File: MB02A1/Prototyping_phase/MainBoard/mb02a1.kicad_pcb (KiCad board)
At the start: 2 copper layers, 71 parts, among them J1 USB_B_Mini, J2 USB_B_Mini, J3 USB_B_Mini, J4 USB_B_Mini, Q1 BC369, Q2 BC369, U1 CH340G, U2 CH340G, U3 CH340G, U4 AMS1117-3.3, U5 W25Q64JVS, U6 25LC256, U7 25LC640, U8 NUCLEO-F446RE, X1 12MHz, X2 12MHz, X3 12MHz

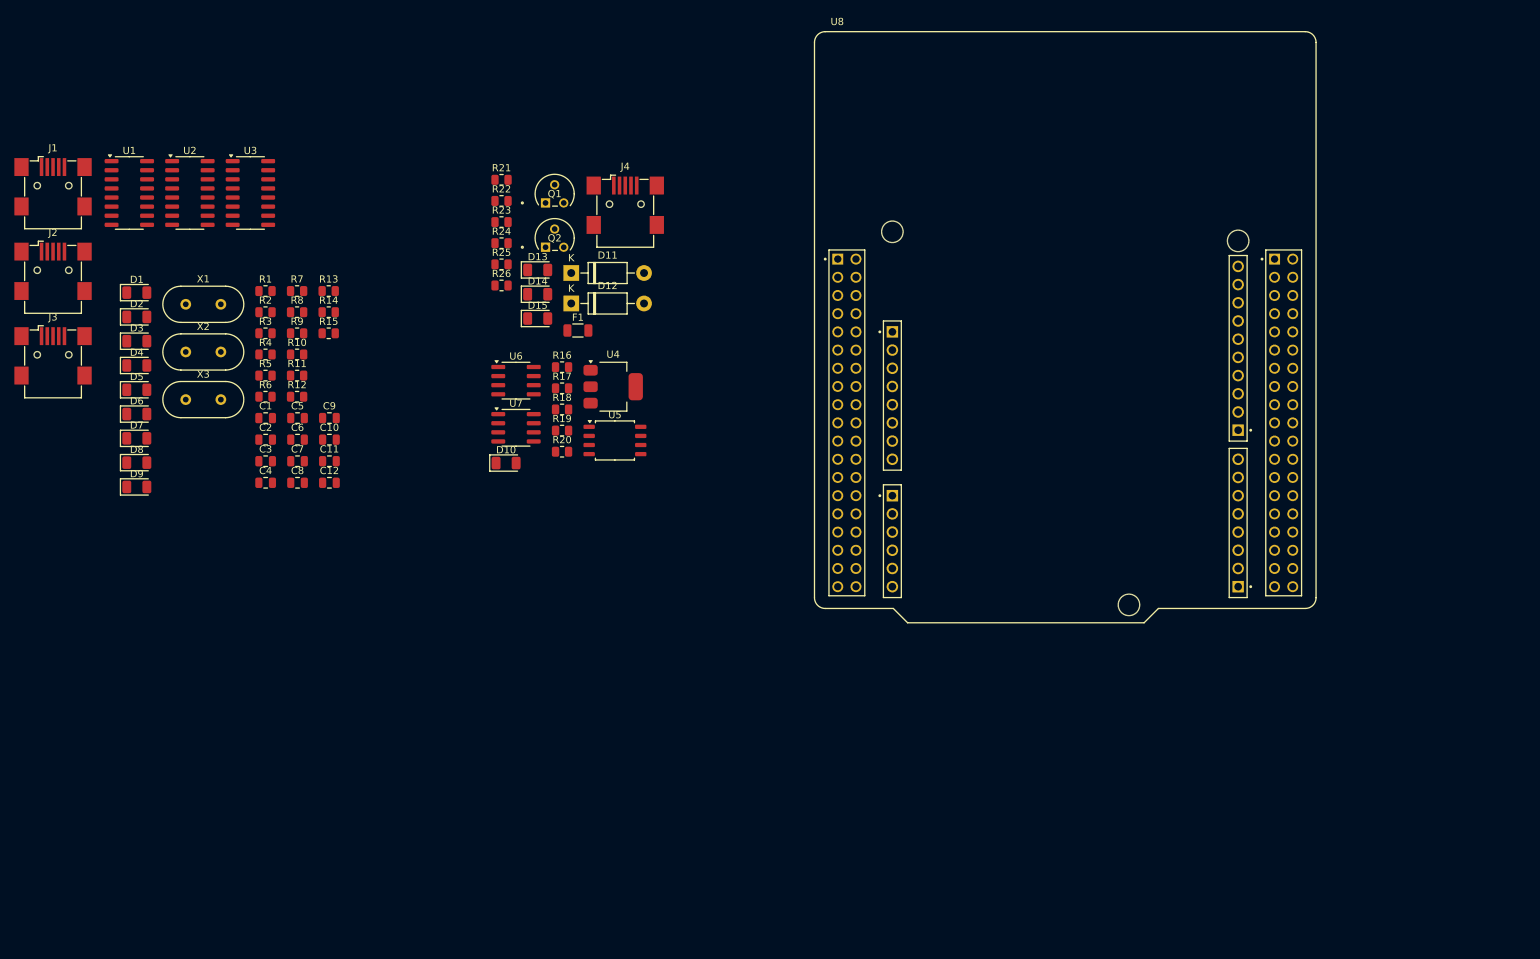
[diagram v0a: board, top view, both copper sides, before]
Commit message: Datasheets added, design updated.
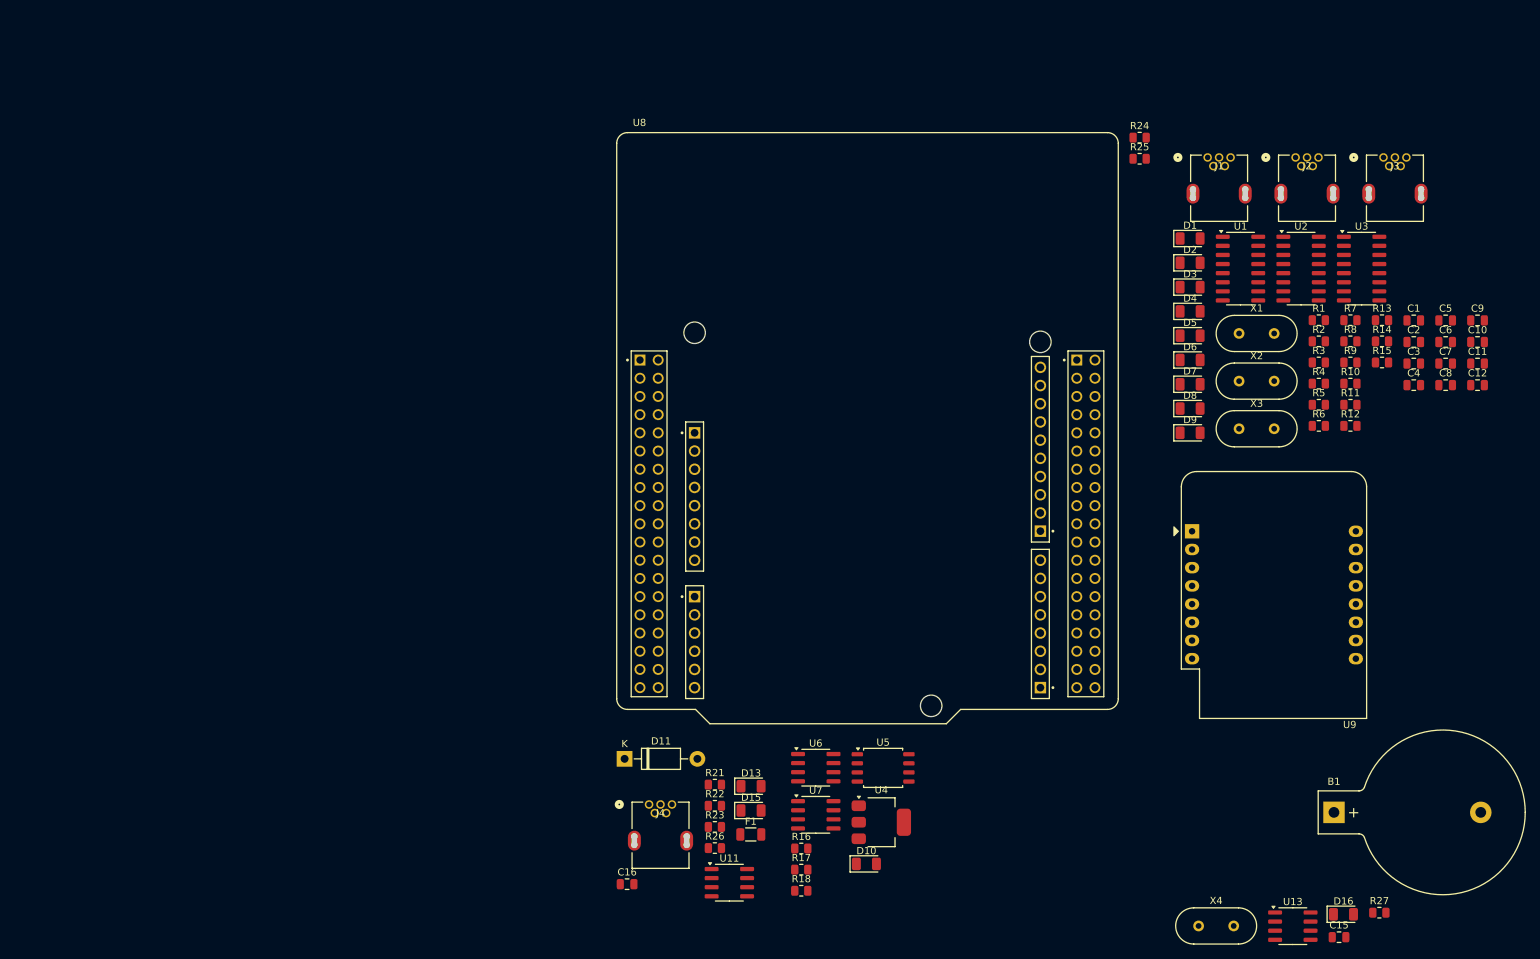
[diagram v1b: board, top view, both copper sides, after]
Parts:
- removed D12: ZY5.6, Diode_THT:D_DO-41_SOD81_P10.16mm_Horizontal
- removed D14: LED, LED_SMD:LED_1206_3216Metric
- removed Q1, Q2: BC369, footprints:TO-92_ONS
- removed R19: 1k, Resistor_SMD:R_0805_2012Metric
- removed R20: 2k, Resistor_SMD:R_0805_2012Metric
- added B1: BC2032-E2, Battery:BatteryHolder_Keystone_103_1x20mm, F.Cu at (251.8, 135.0)
- added C15: 100p, Capacitor_SMD:C_0805_2012Metric, F.Cu at (252.5, 152.4)
- added C16: 1n, Capacitor_SMD:C_0805_2012Metric, F.Cu at (153.1, 145.0)
- added D16: D_Schottky, Diode_SMD:D_1206_3216Metric, F.Cu at (253.1, 149.2)
- added R27: 1k, Resistor_SMD:R_0805_2012Metric, F.Cu at (258.1, 149.0)
- added U11: ACS712-05B, Package_SO:SOIC-8_3.9x4.9mm_P1.27mm, F.Cu at (167.4, 144.8)
- added U13: DS1307Z+, Package_SO:SOIC-8_3.9x4.9mm_P1.27mm, F.Cu at (246.0, 150.9)
- added U9: WEMOS_D1_mini, RF_Module:WEMOS_D1_mini_light, F.Cu at (231.9, 95.8)
- added X4: 32.768 kHz, Crystal:Crystal_HC18-U_Vertical, F.Cu at (232.9, 150.8)
- J1, J2, J3, J4: value USB_B_Mini -> USB B mini; footprint Connector_USB:USB_Mini-B_Wuerth_65100516121_Horizontal -> USB_B_mini_th:54819-0519_MOL
- R22: value 220R -> 10k
- R23: value 2k7 -> 10k
- R24: value 6k8 -> 4k7
- R25: value 470R -> 4k7
- moved J3 187.7 mm to (258.7, 43.6)
- moved J2 174.1 mm to (246.4, 43.6)
- moved J1 161.2 mm to (234.1, 43.6)
- moved C10 160.8 mm to (271.8, 69.3)
- moved C11 160.8 mm to (271.8, 72.4)
- moved C12 160.8 mm to (271.8, 75.4)
- moved C9 160.8 mm to (271.8, 66.3)
- moved C1 160.8 mm to (262.9, 66.3)
- moved C2 160.8 mm to (262.9, 69.3)
- moved C3 160.8 mm to (262.9, 72.4)
- moved C4 160.8 mm to (262.9, 75.4)
- moved C5 160.8 mm to (267.3, 66.3)
- moved C6 160.8 mm to (267.3, 69.3)
- moved C7 160.8 mm to (267.3, 72.4)
- moved C8 160.8 mm to (267.3, 75.4)
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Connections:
- net W25Q64_NCS0V3 renamed W25Q64_NCS3V3
- D10 pad 2: P5V_MEM -> M5V
- J1 pad 6: unconnected-(J1-Shield-Pad6) -> (no net)
- J2 pad 6: unconnected-(J2-Shield-Pad6) -> (no net)
- J3 pad 6: unconnected-(J3-Shield-Pad6) -> (no net)
- J4 pad 6: unconnected-(J4-Shield-Pad6) -> (no net)
- R22 pad 1: Net-(D12-K) -> U_PWR_MEAS
- R22 pad 2: Net-(D14-A) -> Net-(D11-K)
- R23 pad 1: Net-(D12-K) -> GND
- R23 pad 2: Net-(D11-K) -> U_PWR_MEAS
- R24 pad 1: Net-(D12-K) -> M5V
- R24 pad 2: Net-(Q1-B) -> I2C1_SDA
- R25 pad 1: GND -> M5V
- R25 pad 2: Net-(Q1-C) -> I2C1_SCL
- U4 pad 3: P5V_MEM -> M5V
- U5 pad 7: W25Q64_NRST0V3 -> Net-(U4-VO)
- U6 pad 3: P5V_MEM -> M5V
- U6 pad 7: 25LC256_NRST -> M5V
- U6 pad 8: P5V_MEM -> M5V
- U7 pad 3: P5V_MEM -> M5V
- U7 pad 7: 25LC640_NRST -> M5V
- U7 pad 8: P5V_MEM -> M5V
- U8 pad CN10_17: unconnected-(U8B-PB6-PadCN10_17) -> I2C1_SCL
- U8 pad CN10_19: unconnected-(U8B-PC7-PadCN10_19) -> SPI2_SCK
- U8 pad CN10_21: unconnected-(U8B-PA9-PadCN10_21) -> USART1_TX
- U8 pad CN10_22: unconnected-(U8B-PB2-PadCN10_22) -> 25LC256_NCS
- U8 pad CN10_24: unconnected-(U8B-PB1-PadCN10_24) -> 25LC640_NCS
- U8 pad CN10_28: unconnected-(U8B-PB14-PadCN10_28) -> WEMOS_RST
- U8 pad CN10_33: unconnected-(U8B-PA10-PadCN10_33) -> USART1_RX
- U8 pad CN6_5: unconnected-(U8C-CN6_+5V-PadCN6_5) -> M5V
- U8 pad CN7_19: Net-(U8A-CN7_GND-PadCN7_19) -> GND
- U8 pad CN7_20: Net-(U8A-CN7_GND-PadCN7_19) -> GND
- U8 pad CN7_21: unconnected-(U8A-PB7-PadCN7_21) -> I2C1_SDA
- U8 pad CN7_22: Net-(U8A-CN7_GND-PadCN7_19) -> GND
- U8 pad CN7_28: unconnected-(U8A-PA0-PadCN7_28) -> UART4_TX
- U8 pad CN7_3: unconnected-(U8A-PC12-PadCN7_3) -> UART5_TX
- U8 pad CN7_30: unconnected-(U8A-PA1-PadCN7_30) -> UART4_RX
- U8 pad CN7_34: unconnected-(U8A-PB0-PadCN7_34) -> W25Q64_NCS
- U8 pad CN7_35: unconnected-(U8A-PC2-PadCN7_35) -> SPI2_MISO
- U8 pad CN7_36: unconnected-(U8A-PC1/PB9-PadCN7_36) -> SPI2_MOSI
- U8 pad CN7_37: unconnected-(U8A-PC3-PadCN7_37) -> I_PWR_MEAS
- U8 pad CN7_38: unconnected-(U8A-PC0/PB8-PadCN7_38) -> U_PWR_MEAS
- U8 pad CN7_4: unconnected-(U8A-PD2-PadCN7_4) -> UART5_RX
- U8 pad CN7_6: unconnected-(U8A-E5V-PadCN7_6) -> 5V_REG
- U8 pad CN7_8: Net-(U8A-CN7_GND-PadCN7_19) -> GND
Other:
- board outline added: 7.3 x 1.2 mm

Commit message: Design update, production preparation.
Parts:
- removed C15: 100p, Capacitor_SMD:C_0805_2012Metric
- removed C16: 1n, Capacitor_SMD:C_0805_2012Metric
- removed D16: D_Schottky, Diode_SMD:D_1206_3216Metric
- removed R27: 1k, Resistor_SMD:R_0805_2012Metric
- removed U13: DS1307Z+, Package_SO:SOIC-8_3.9x4.9mm_P1.27mm
- removed X4: 32.768 kHz, Crystal:Crystal_HC18-U_Vertical
- added ?: , , F.Cu at (80.5, 49.7)
- added ?: , , F.Cu at (80.5, 150.0)
- added ?: , , F.Cu at (205.8, 150.0)
- added ?: , , F.Cu at (205.8, 50.0)
- added ADC.1: Conn_01x02_Pin, Connector_PinHeader_2.54mm:PinHeader_1x02_P2.54mm_Vertical, F.Cu at (199.0, 83.8)
- added ADC.2: Conn_01x02_Pin, Connector_PinHeader_2.54mm:PinHeader_1x02_P2.54mm_Vertical, F.Cu at (204.8, 83.8)
- added C13: 100n, Capacitor_SMD:C_0805_2012Metric, F.Cu at (126.2, 94.6)
- added D12: LED, LED_SMD:LED_1206_3216Metric, F.Cu at (81.6, 143.9)
- added D14: LED, LED_SMD:LED_1206_3216Metric, F.Cu at (100.1, 147.5)
- added DAC.1: Conn_01x02_Pin, Connector_PinHeader_2.54mm:PinHeader_1x02_P2.54mm_Vertical, F.Cu at (198.8, 63.5)
- added DISPLAY1: Conn_01x14_Pin, Connector_PinHeader_2.54mm:PinHeader_1x14_P2.54mm_Vertical, F.Cu at (193.0, 53.3)
- added EXIO.1: Conn_01x08_Pin, Connector_PinHeader_2.54mm:PinHeader_1x08_P2.54mm_Vertical, F.Cu at (204.3, 128.7)
- added EXIO.2: Conn_01x08_Pin, Connector_PinHeader_2.54mm:PinHeader_1x08_P2.54mm_Vertical, F.Cu at (204.3, 134.9)
- added EXTI.1: Conn_01x02_Pin, Connector_PinHeader_2.54mm:PinHeader_1x02_P2.54mm_Vertical, F.Cu at (204.8, 63.5)
- added EXTI.2: Conn_01x02_Pin, Connector_PinHeader_2.54mm:PinHeader_1x02_P2.54mm_Vertical, F.Cu at (198.8, 73.8)
- added EXTI.3: Conn_01x02_Pin, Connector_PinHeader_2.54mm:PinHeader_1x02_P2.54mm_Vertical, F.Cu at (204.8, 73.8)
- added I2C1.1: Conn_01x04_Pin, Connector_PinHeader_2.54mm:PinHeader_1x04_P2.54mm_Vertical, F.Cu at (178.8, 128.9)
- added I2C1.2: Conn_01x04_Pin, Connector_PinHeader_2.54mm:PinHeader_1x04_P2.54mm_Vertical, F.Cu at (178.8, 134.9)
- added I2C1.3: Conn_01x04_Pin, Connector_PinHeader_2.54mm:PinHeader_1x04_P2.54mm_Vertical, F.Cu at (178.8, 140.9)
- added I2C1.4: Conn_01x04_Pin, Connector_PinHeader_2.54mm:PinHeader_1x04_P2.54mm_Vertical, F.Cu at (178.8, 146.9)
- added PWM.1: Conn_01x02_Pin, Connector_PinHeader_2.54mm:PinHeader_1x02_P2.54mm_Vertical, F.Cu at (193.2, 116.0)
- added PWM.2: Conn_01x02_Pin, Connector_PinHeader_2.54mm:PinHeader_1x02_P2.54mm_Vertical, F.Cu at (199.0, 116.0)
- added PWM.3: Conn_01x02_Pin, Connector_PinHeader_2.54mm:PinHeader_1x02_P2.54mm_Vertical, F.Cu at (204.8, 116.0)
- added PWR3V3.1: Conn_01x02_Pin, Connector_PinHeader_2.54mm:PinHeader_1x02_P2.54mm_Vertical, F.Cu at (193.2, 105.2)
- added PWR3V3.2: Conn_01x02_Pin, Connector_PinHeader_2.54mm:PinHeader_1x02_P2.54mm_Vertical, F.Cu at (199.0, 105.3)
- added PWR3V3.3: Conn_01x02_Pin, Connector_PinHeader_2.54mm:PinHeader_1x02_P2.54mm_Vertical, F.Cu at (204.8, 105.3)
- added PWR5V.1: Conn_01x02_Pin, Connector_PinHeader_2.54mm:PinHeader_1x02_P2.54mm_Vertical, F.Cu at (193.2, 94.5)
- added PWR5V.2: Conn_01x02_Pin, Connector_PinHeader_2.54mm:PinHeader_1x02_P2.54mm_Vertical, F.Cu at (199.0, 94.5)
- added PWR5V.3: Conn_01x02_Pin, Connector_PinHeader_2.54mm:PinHeader_1x02_P2.54mm_Vertical, F.Cu at (204.8, 94.5)
- added R19: 1k5, Resistor_SMD:R_0805_2012Metric, F.Cu at (87.6, 135.6)
- added R20: 1k, Resistor_SMD:R_0805_2012Metric, F.Cu at (161.8, 97.8)
- added SPI2.1: Conn_01x06_Pin, Connector_PinHeader_2.54mm:PinHeader_1x06_P2.54mm_Vertical, F.Cu at (199.1, 140.9)
- added SPI2.2: Conn_01x06_Pin, Connector_PinHeader_2.54mm:PinHeader_1x06_P2.54mm_Vertical, F.Cu at (199.1, 147.0)
- added U10: WEMOS_D1_mini, RF_Module:WEMOS_D1_mini_light, F.Cu at (114.8, 147.5)
- added U12: MCP23017_SO, Package_SO:SOIC-28W_7.5x17.9mm_P1.27mm, F.Cu at (167.8, 73.4)
- C1: value 22p -> 1n
- C10, C9: value 22p -> 100n
- C3, C4, C7: value 100n -> 22p
- D11: value 1N4001 -> LED; footprint Diode_THT:D_DO-41_SOD81_P10.16mm_Horizontal -> LED_SMD:LED_1206_3216Metric
- D2: value LED -> 1N4001; footprint LED_SMD:LED_1206_3216Metric -> Diode_THT:D_DO-41_SOD81_P10.16mm_Horizontal
- R1: value 1k5 -> 220R
- R17: value 1k -> 1k5
- R18: value 2k -> 1k5
- R2, R3: value 1k5 -> 10k
- R21: value 220R -> 2k
- R22, R23: value 10k -> 4k7
- R24, R25: value 4k7 -> 1k5
- U1: value CH340G -> ACS712-05B; footprint Package_SO:SOIC-16_3.9x9.9mm_P1.27mm -> Package_SO:SOIC-8_3.9x4.9mm_P1.27mm
- U11: value ACS712-05B -> DS3231M; footprint Package_SO:SOIC-8_3.9x4.9mm_P1.27mm -> Package_SO:SOIC-16W_7.5x10.3mm_P1.27mm
- U4: value AMS1117-3.3 -> CH340G; footprint Package_TO_SOT_SMD:SOT-223-3_TabPin2 -> Package_SO:SOIC-16_3.9x9.9mm_P1.27mm
- U5: value W25Q64JVS -> AMS1117-3.3; footprint Package_SO:SOIC-8_5.23x5.23mm_P1.27mm -> Package_TO_SOT_SMD:SOT-223-3_TabPin2
- U6: value 25LC256 -> W25Q64JVS; footprint Package_SO:SOIC-8_3.9x4.9mm_P1.27mm -> Package_SO:SOIC-8_5.23x5.23mm_P1.27mm
- U7: value 25LC640 -> 25LC256
- U8: value NUCLEO-F446RE -> 25LC640; footprint NUCLEO-F446RE:MODULE_NUCLEO-F446RE -> Package_SO:SOIC-8_3.9x4.9mm_P1.27mm
- U9: value WEMOS_D1_mini -> NUCLEO-F446RE; footprint RF_Module:WEMOS_D1_mini_light -> NUCLEO-F446RE:MODULE_NUCLEO-F446RE
- X1, X2, X3: value 12MHz -> 12 MHz; footprint Crystal:Crystal_HC18-U_Vertical -> Crystal:Crystal_HC49-U_Vertical
- moved C7 188.1 mm to (93.4, 143.9)
- moved R13 186.0 mm to (87.6, 139.9)
- moved C6 180.8 mm to (93.4, 118.7)
- moved J3 180.7 mm to (87.3, 101.0), turned to -90 degrees
- moved R15 177.1 mm to (87.6, 118.9)
- moved C5 176.1 mm to (93.4, 93.7)
- moved R14 172.5 mm to (87.7, 93.9)
- moved C1 170.3 mm to (92.7, 68.9)
- moved R12 169.8 mm to (87.6, 114.9)
- moved R11 166.6 mm to (87.8, 90.1)
- moved U3 163.9 mm to (97.7, 102.9)
- moved D6 163.1 mm to (81.6, 135.6)
- moved R4 162.4 mm to (87.6, 64.9)
- moved J2 162.4 mm to (87.3, 75.9), turned to -90 degrees
- moved R1 162.1 mm to (87.6, 68.9)
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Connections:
- B1 pad 1: Net-(D16-A) -> Net-(U11-VBAT)
- C1 pad 1: Net-(U1-XI) -> Net-(U1-FILTER)
- C10 pad 1: Net-(U3-XO) -> Net-(U4-V3)
- C11 pad 1: Net-(U3-V3) -> VBUS1
- C12 pad 1: VBUS3 -> VBUS2
- C2 pad 1: Net-(U1-XO) -> Net-(U2-XI)
- C3 pad 1: Net-(U1-V3) -> Net-(U3-XI)
- C4 pad 1: VBUS1 -> Net-(U4-XI)
- C5 pad 1: Net-(U2-XI) -> Net-(U2-XO)
- C6 pad 1: Net-(U2-XO) -> Net-(U3-XO)
- C7 pad 1: Net-(U2-V3) -> Net-(U4-XO)
- C8 pad 1: VBUS2 -> Net-(U2-V3)
- C9 pad 1: Net-(U3-XI) -> Net-(U3-V3)
- D1 pad 2: VBUS1 -> Net-(D1-A)
- D10 pad 2: M5V -> VBUS1
- D11 pad 2: GND -> VBUS2
- D13 pad 1: Net-(D11-K) -> Net-(D13-K)
- D15 pad 2: 5V_REG -> Net-(D15-A)
- D2 pad 1: Net-(D2-K) -> Net-(D1-K)
- D2 pad 2: VBUS1 -> GND
- D3 pad 2: VBUS1 -> 5V_REG
- D4 pad 2: VBUS2 -> VBUS1
- D6 pad 2: VBUS2 -> VBUS3
- D7 pad 2: VBUS3 -> VBUS1
- D8 pad 2: VBUS3 -> VBUS2
- F1 pad 1: Net-(J4-VBUS) -> Net-(J1-VBUS)
- F1 pad 2: Net-(D11-K) -> Net-(D1-K)
- J1 pad 1: VBUS1 -> Net-(J1-VBUS)
- J1 pad 2: D1- -> unconnected-(J1-D--Pad2)
- J1 pad 3: D1+ -> unconnected-(J1-D+-Pad3)
- J2 pad 1: VBUS2 -> VBUS1
- J2 pad 2: D2- -> D1-
- J2 pad 3: D2+ -> D1+
- J3 pad 1: VBUS3 -> VBUS2
- J3 pad 2: D3- -> D2-
- J3 pad 3: D3+ -> D2+
- J4 pad 1: Net-(J4-VBUS) -> VBUS3
- J4 pad 2: unconnected-(J4-D--Pad2) -> D3-
- J4 pad 3: unconnected-(J4-D+-Pad3) -> D3+
- R1 pad 1: Net-(U1-TXD) -> Net-(J1-VBUS)
- R1 pad 2: USART1_RX -> Net-(D1-A)
- R10 pad 1: Net-(D6-K) -> Net-(U4-RXD)
- R10 pad 2: UART5_TX -> WUART1_TX
- R11 pad 1: Net-(U3-TXD) -> Net-(D4-K)
- R11 pad 2: WUART1_RX -> GND
- R12 pad 1: Net-(U3-RXD) -> Net-(D5-K)
- R12 pad 2: WUART1_TX -> GND
- R13 pad 1: Net-(D7-K) -> Net-(D6-K)
- R14 pad 1: Net-(D8-K) -> Net-(D7-K)
- R14 pad 2: WUART1_RX -> USART1_RX
- R15 pad 1: Net-(D9-K) -> Net-(D8-K)
- R15 pad 2: WUART1_TX -> UART5_RX
- R16 pad 1: Net-(D10-K) -> Net-(D9-K)
- R16 pad 2: GND -> WUART1_RX
- R17 pad 1: W25Q64_NCS -> Net-(D10-K)
- R17 pad 2: W25Q64_NCS3V3 -> USART1_TX
- R18 pad 1: W25Q64_NCS3V3 -> Net-(D11-K)
- R18 pad 2: GND -> UART5_TX
- R2 pad 1: Net-(U1-RXD) -> U_PWR_MEAS
- R2 pad 2: USART1_TX -> Net-(D1-K)
- R21 pad 1: Net-(J4-VBUS) -> W25Q64_NCS3V3
- R21 pad 2: Net-(D13-A) -> GND
- R22 pad 1: U_PWR_MEAS -> M5V
- R22 pad 2: Net-(D11-K) -> I2C1_SDA
- R23 pad 1: GND -> M5V
- R23 pad 2: U_PWR_MEAS -> I2C1_SCL
- R24 pad 1: M5V -> Net-(D13-K)
- R24 pad 2: I2C1_SDA -> GND
- R25 pad 1: M5V -> Net-(D14-K)
- R25 pad 2: I2C1_SCL -> GND
- R26 pad 1: GND -> Net-(D15-K)
- R26 pad 2: Net-(D15-K) -> GND
- R3 pad 1: Net-(D1-K) -> GND
- R3 pad 2: GND -> U_PWR_MEAS
- R4 pad 1: Net-(D2-K) -> GND
- R4 pad 2: USART1_RX -> Net-(D3-K)
- R5 pad 1: Net-(D3-K) -> Net-(U2-TXD)
- R5 pad 2: USART1_TX -> USART1_RX
- R6 pad 1: Net-(U2-TXD) -> Net-(U2-RXD)
- R6 pad 2: UART5_RX -> USART1_TX
- R7 pad 1: Net-(U2-RXD) -> Net-(U3-TXD)
- R7 pad 2: UART5_TX -> UART5_RX
- R8 pad 1: Net-(D4-K) -> Net-(U3-RXD)
- R8 pad 2: GND -> UART5_TX
- R9 pad 1: Net-(D5-K) -> Net-(U4-TXD)
- R9 pad 2: UART5_RX -> WUART1_RX
- U1 pad 1: GND -> 5V_REG
- U1 pad 2: Net-(U1-TXD) -> 5V_REG
- U1 pad 3: Net-(U1-RXD) -> Net-(D1-K)
- U1 pad 4: Net-(U1-V3) -> Net-(D1-K)
- U1 pad 5: D1+ -> GND
- U1 pad 6: D1- -> Net-(U1-FILTER)
- U1 pad 7: Net-(U1-XI) -> I_PWR_MEAS
- U1 pad 8: Net-(U1-XO) -> M5V
- U11 pad 1: 5V_REG -> unconnected-(U11-32KHZ-Pad1)
- U11 pad 2: 5V_REG -> M5V
- U11 pad 3: Net-(D11-K) -> unconnected-(U11-~{INT}/SQW-Pad3)
- U11 pad 4: Net-(D11-K) -> unconnected-(U11-~{RST}-Pad4)
- U11 pad 6: Net-(U11-FILTER) -> GND
- U11 pad 7: I_PWR_MEAS -> GND
- U11 pad 8: M5V -> GND
- U2 pad 16: VBUS2 -> VBUS1
- U2 pad 5: D2+ -> D1+
- U2 pad 6: D2- -> D1-
- U3 pad 16: VBUS3 -> VBUS2
- U3 pad 5: D3+ -> D2+
- U3 pad 6: D3- -> D2-
- U4 pad 2: Net-(U4-VO) -> Net-(U4-TXD)
- U4 pad 3: M5V -> Net-(U4-RXD)
- U5 pad 1: W25Q64_NCS3V3 -> GND
- U5 pad 2: SPI2_MISO -> Net-(U5-VO)
- U5 pad 3: Net-(U4-VO) -> M5V
- U6 pad 1: 25LC256_NCS -> W25Q64_NCS3V3
- U6 pad 3: M5V -> Net-(U5-VO)
- U6 pad 7: M5V -> Net-(U5-VO)
- U6 pad 8: M5V -> Net-(U5-VO)
- U7 pad 1: 25LC640_NCS -> 25LC256_NCS
- X1 pad 1: Net-(U1-XO) -> Net-(U2-XO)
- X1 pad 2: Net-(U1-XI) -> Net-(U2-XI)
- X2 pad 1: Net-(U2-XO) -> Net-(U3-XO)
- X2 pad 2: Net-(U2-XI) -> Net-(U3-XI)
- X3 pad 1: Net-(U3-XO) -> Net-(U4-XO)
- X3 pad 2: Net-(U3-XI) -> Net-(U4-XI)
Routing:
- net GND: track 0.00 -> 753.6 mm, vias 0 -> 9
- net 5V_REG: track 0.00 -> 335.2 mm, vias 0 -> 2
- net M5V: track 0.00 -> 212.2 mm, vias 0 -> 5
- net I2C1_SCL: track 0.00 -> 166.4 mm, vias 0 -> 3
- net SPI2_SCK: track 0.00 -> 159.9 mm, vias 0 -> 4
- net WEMOS_RST: track 0.00 -> 150.9 mm, vias 0 -> 1
- net SPI2_CS1: track 0.00 -> 149.9 mm, vias 0 -> 1
- net SPI2_MOSI: track 0.00 -> 141.0 mm, vias 0 -> 3
- net SPI2_CS0: track 0.00 -> 139.1 mm, vias 0 -> 1
- net U_PWR_MEAS: track 0.00 -> 137.6 mm, vias 0 -> 2
- net USART1_RX: track 0.00 -> 133.4 mm, vias 0 -> 3
- net SPI2_MISO: track 0.00 -> 133.1 mm, vias 0 -> 3
- net I2C1_SDA: track 0.00 -> 128.3 mm, vias 0 -> 3
- net I_PWR_MEAS: track 0.00 -> 125.4 mm, vias 0 -> 2
- net PWM3: track 0.00 -> 123.8 mm, vias 0 -> 1
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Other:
- board size 7.3 x 1.2 mm -> 130 x 105 mm
- board text added: "2025-04-04"
- board text added: "MB02A1"
- board text added: "© Ahmed Ibrahim Gazar"
